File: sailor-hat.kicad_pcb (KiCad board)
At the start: 2 copper layers, 65 x 56 mm, 96 parts, among them J1 Screw_Terminal_01x04, J2 Raspberry_Pi_2_3, J3 Conn_02x07_Counter_Clockwise, J4 Screw_Terminal_01x02, J5 Screw_Terminal_01x03, J6 Conn_02x02_Odd_Even, Q1 DMP3098L, SW1 SW_SPST, U1 ATtiny841-SSU, U2 TPS61022, U3 H7533-H#, U4 DS3231MZ, U5 MCP2515-xST, U6 ISO1050DUB, U7 H7550-H#, U8 TX4138, Y1 1C208000BC0R

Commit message: Cram all new stuff on the PCB
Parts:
- removed D14: PSBD521S-40, Diode_SMD:D_SOD-523
- removed J6: Conn_02x02_Odd_Even, Connector_PinHeader_2.54mm:PinHeader_2x02_P2.54mm_Vertical
- removed R29, R30: 13k, Resistor_SMD:R_0603_1608Metric
- removed R31: 100k, Resistor_SMD:R_0603_1608Metric
- added C15: 2.2uF 16V, Capacitor_SMD:C_0603_1608Metric, F.Cu at (34.3, 67.4)
- added D10: SMBJ36CA, Diode_SMD:D_SMB, F.Cu at (38.4, 57.3)
- added D6: RB521S-30, Diode_SMD:D_SOD-523, F.Cu at (48.9, 59.3)
- added JP2: Jumper_2_Open, Connector_PinHeader_2.54mm:PinHeader_1x02_P2.54mm_Vertical, F.Cu at (36.5, 53.2)
- added JP3: Jumper_2_Open, Connector_PinHeader_2.54mm:PinHeader_1x02_P2.54mm_Vertical, F.Cu at (40.2, 53.2)
- added R22: 15k, Resistor_SMD:R_0603_1608Metric, F.Cu at (46.6, 58.4)
- added R25: 7.5k, Resistor_SMD:R_0603_1608Metric, F.Cu at (46.6, 59.9)
- added U9: INA199A1DCKR, Package_TO_SOT_SMD:SOT-363_SC-70-6_Handsoldering, F.Cu at (47.0, 38.0)
- C11: value 2.2uF 16V -> 2.2uF 50V; footprint Capacitor_SMD:C_0603_1608Metric -> Capacitor_SMD:C_1206_3216Metric
- C4: value 22pF -> 12pF
- C7: value 220pF -> 100nF
- C8: value 2.2uF 50V -> 1nF; footprint Capacitor_SMD:C_1206_3216Metric -> Capacitor_SMD:C_0603_1608Metric
- D1: value 5.0SMDJ20CA -> 5.0SMDJ36CA
- D13: value SMBJ20CA -> SS210; footprint Diode_SMD:D_SMB -> Diode_SMD:D_SMA
- D8: value MM3Z10 -> MM3Z8V2
- Q1: value DMP3098L -> WST03P06
- R17: value 13k -> 39k
- R20: value 100k -> 200k
- moved R23 13.6 mm to (47.1, 40.8), turned to 0 degrees
- moved C8 12.1 mm to (46.6, 61.5), turned to 180 degrees
- moved C7 11.0 mm to (47.2, 35.8)
- moved G*** 6.41 mm to (55.6, 63.2)
- moved C11 5.07 mm to (33.5, 60.8), turned to 90 degrees
- moved C27 4.84 mm to (73.7, 50.7), turned to 0 degrees
- moved U4 4.58 mm to (72.3, 55.1)
- moved L2 3.06 mm to (37.8, 37.3)
- moved D13 2.89 mm to (38.4, 61.4), turned to 0 degrees
- moved R20 2.69 mm to (53.3, 31.2), turned to 0 degrees
- moved C19 2.17 mm to (37.3, 31.9)
- moved R16 2.17 mm to (34.7, 30.5)
- moved C13 2.07 mm to (56.9, 49.1)
- moved F2 2.04 mm to (33.3, 54.5), turned to 90 degrees
- moved U2 1.80 mm to (41.0, 31.6)
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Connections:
- C10 pad 1: /CANbus interface/CAN_5V -> /CAN_5V
- C11 pad 1: /CANbus interface/CAN_5V -> /Protection/CAN12V_prot
- C16 pad 1: /Vcap -> /Buck converter/Vout
- C4 pad 1: /Vcap -> /Buck converter/Vout
- C7 pad 1: 5V -> GND
- C7 pad 2: /Boost converter/FB -> REG3.3V
- C8 pad 1: /CANbus interface/CAN12V_prot -> Net-(C8-Pad1)
- C8 pad 2: /CAN0_GND -> GND
- D13 pad 1: /CANbus interface/CAN12V_fused -> /Protection/CAN12V_prot
- D13 pad 2: /CAN0_GND -> /Protection/CAN12V_fused
- F2 pad 1: /CANbus interface/CAN12V_fused -> /Protection/CAN12V_fused
- L1 pad 2: /Vcap -> /Buck converter/Vout
- R14 pad 1: /Vcap -> /Buck converter/Vout
- R17 pad 2: Net-(R17-Pad2) -> GND
- R20 pad 1: Net-(R20-Pad1) -> /Vcap
- R23 pad 1: /Buck converter/ILIM -> /Vcap
- R23 pad 2: /Control MCU/12V_prot -> /Buck converter/Vout
- U6 pad 8: /CANbus interface/CAN_5V -> /CAN_5V
- U7 pad 2: /CANbus interface/CAN_5V -> /CAN_5V
- U7 pad 3: /CANbus interface/CAN12V_prot -> /Protection/CAN12V_prot
- U8 pad 2: /Buck converter/ILIM -> /Control MCU/12V_prot
- U8 pad 9: /Buck converter/ILIM -> /Control MCU/12V_prot
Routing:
- net REG3.3V: track 25.1 -> 68.6 mm, vias 2 -> 7
- net /Buck converter/Vout: track 0.00 -> 39.0 mm, vias 0 -> 6
- net /Vcap: track 76.7 -> 50.0 mm, vias 2 -> 4
- net /Buck converter/CSAOUT: track 0.00 -> 25.6 mm, vias 0 -> 3
- net /Buck converter/FB: track 5.85 -> 24.1 mm, vias 0 -> 2
- net GND: track 115.5 -> 130.4 mm
- net /CANbus interface/CAN_5V: track 11.3 -> 0.00 mm, vias 2 -> 0
- net /CAN_5V: track 0.00 -> 9.79 mm, vias 0 -> 2
- net /Protection/CAN12V_fused: track 0.00 -> 9.39 mm
- net /V12s: track 58.2 -> 66.6 mm, vias 5 -> 7
- net /CANbus interface/CAN12V_fused: track 6.37 -> 0.00 mm
- net /Control MCU/12V_prot: track 24.7 -> 30.7 mm, vias 0 -> 2
- net 3.3V: track 129.3 -> 123.5 mm, vias 8 -> 7
- net Net-(C8-Pad1): track 0.00 -> 5.32 mm
- net /CANbus interface/CAN12V_prot: track 5.27 -> 0.00 mm
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- added copper zone on B.Cu, net /Control MCU/12V_prot
- removed copper zone on B.Cu, net /Buck converter/ILIM
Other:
- board text added: "Rev.K"
- board text added: "Status"
- board text added: "Vcap"
- board text removed: "Rev.J"
- board text removed: "STA1"
- board text removed: "STA2"

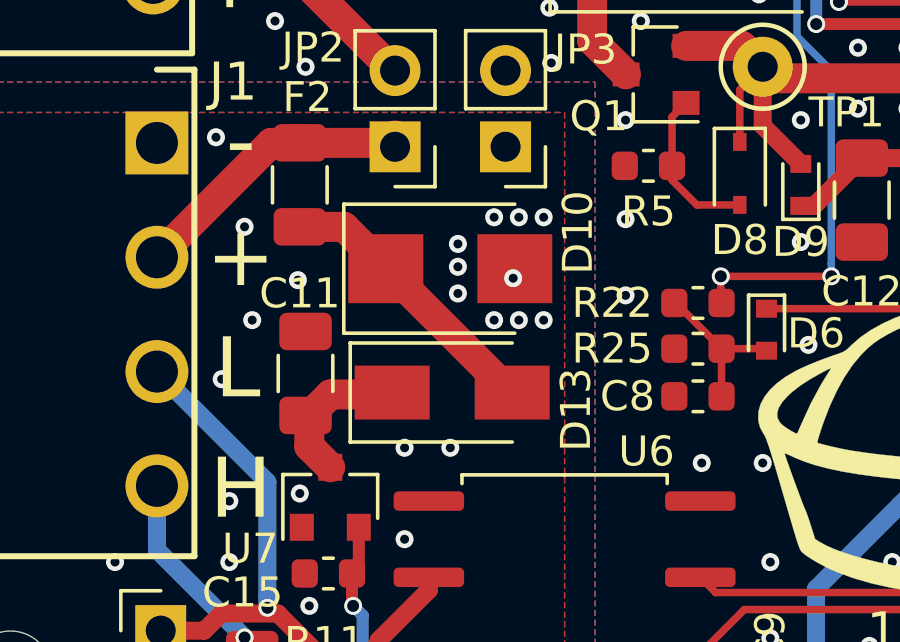
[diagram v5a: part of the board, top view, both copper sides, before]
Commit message: Swap CAN power rectifier diode into a smaller one
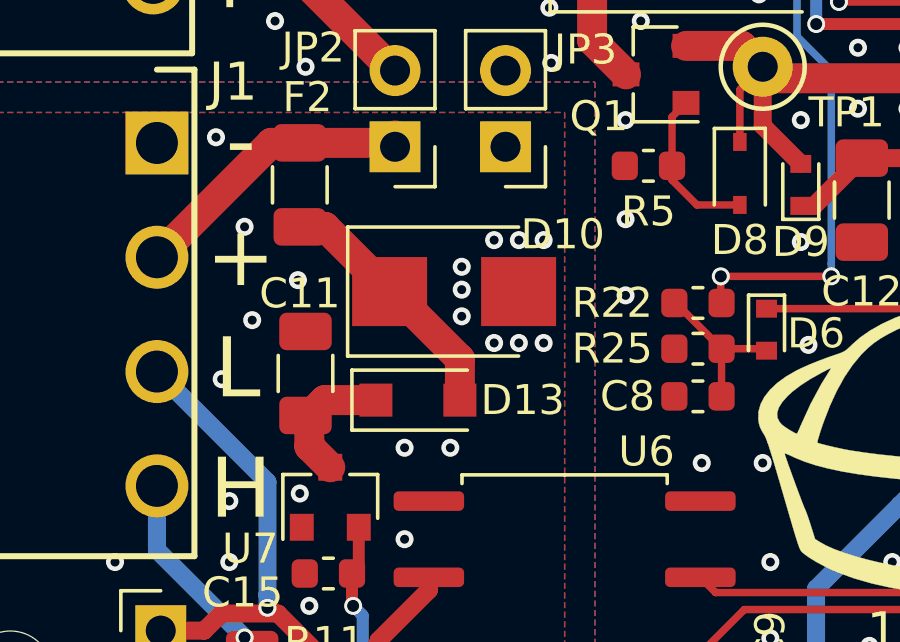
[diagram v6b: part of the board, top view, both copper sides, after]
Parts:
- D13: value SS210 -> SM4007PL; footprint Diode_SMD:D_SMA -> Diode_SMD:D_SOD-123F
- moved D13 1.17 mm to (37.3, 61.7)
- moved D10 0.77 mm to (38.5, 58.0)
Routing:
- net /Protection/CAN12V_fused: track 9.39 -> 8.53 mm
- net /Protection/CAN12V_prot: track 5.07 -> 4.45 mm
- net /CAN0_GND: vias 26 -> 25

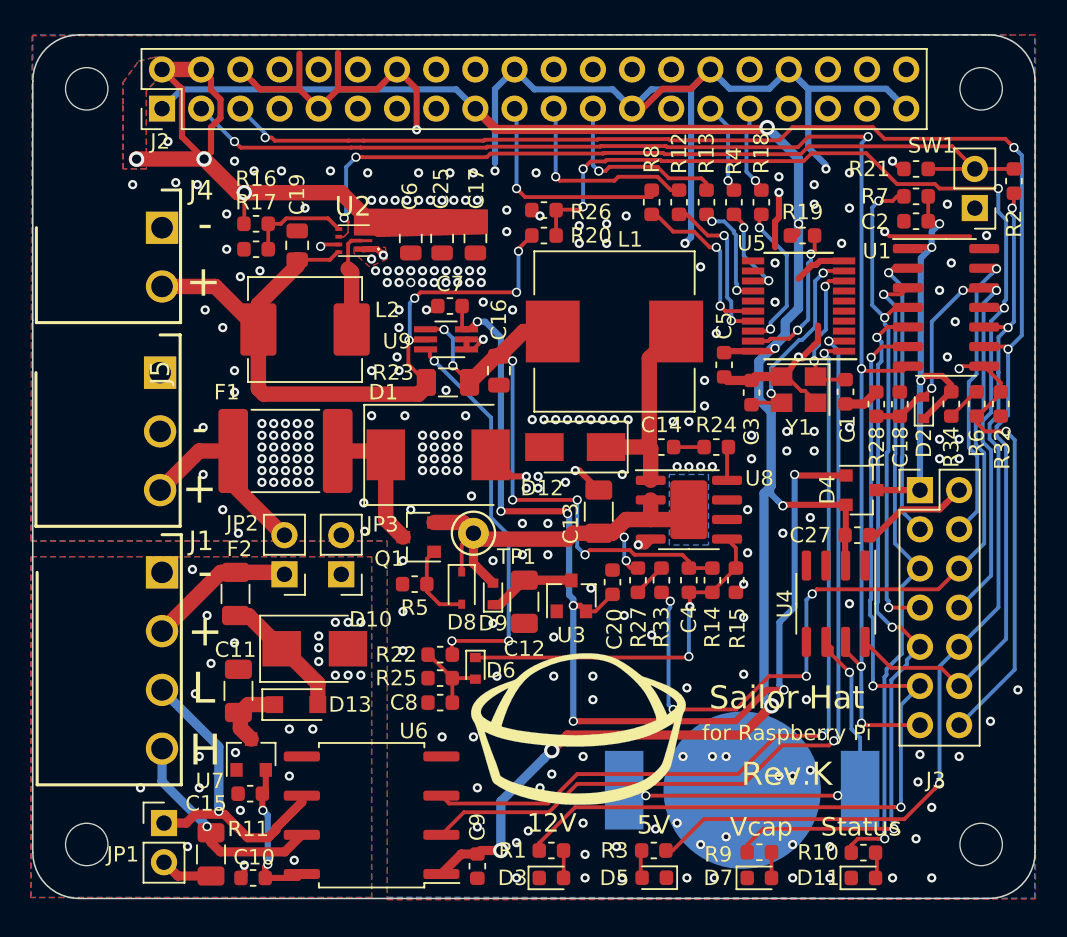
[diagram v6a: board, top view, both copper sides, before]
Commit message: Update components according to JLCPCB availability
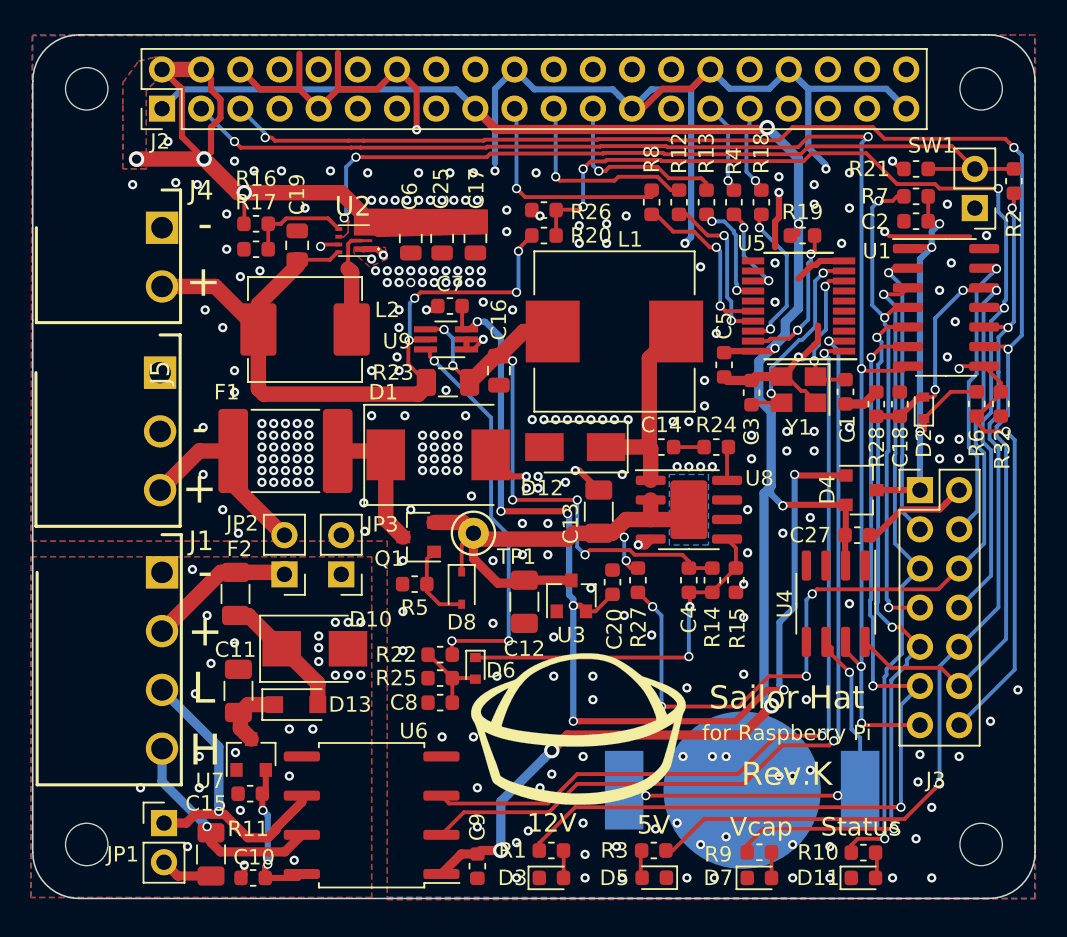
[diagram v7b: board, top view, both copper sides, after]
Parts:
- removed D9: PSBD521S-40, Diode_SMD:D_SOD-523
- removed R33, R34: 100k, Resistor_SMD:R_0603_1608Metric
- D1: value 5.0SMDJ36CA -> 5.0SMDJ33CA
- D10: value SMBJ36CA -> SMBJ33CA
- D6: value RB521S-30 -> PSBD521S-40
- R27: value 100k -> 62k
- R28: value 13k -> 2.2k
- R6: value 100k -> 200k
- Y1: value 1C208000BC0R -> 1C208000CE0Q
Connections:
- C12 pad 1: Net-(C12-Pad1) -> /Control MCU/12V_prot
- R27 pad 2: Net-(R27-Pad2) -> /V12s
- R6 pad 1: Net-(R34-Pad2) -> /ATT_Vcc
- U3 pad 3: Net-(C12-Pad1) -> /Control MCU/12V_prot
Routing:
- net Net-(C12-Pad1): track 5.75 -> 0.00 mm
- net /Control MCU/12V_prot: track 30.7 -> 35.7 mm
- net Net-(R34-Pad2): track 2.30 -> 0.00 mm
- net Net-(R27-Pad2): track 2.21 -> 0.00 mm
- net /V12s: track 66.6 -> 67.8 mm

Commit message: Redesigned layout to take EMC issues better into account
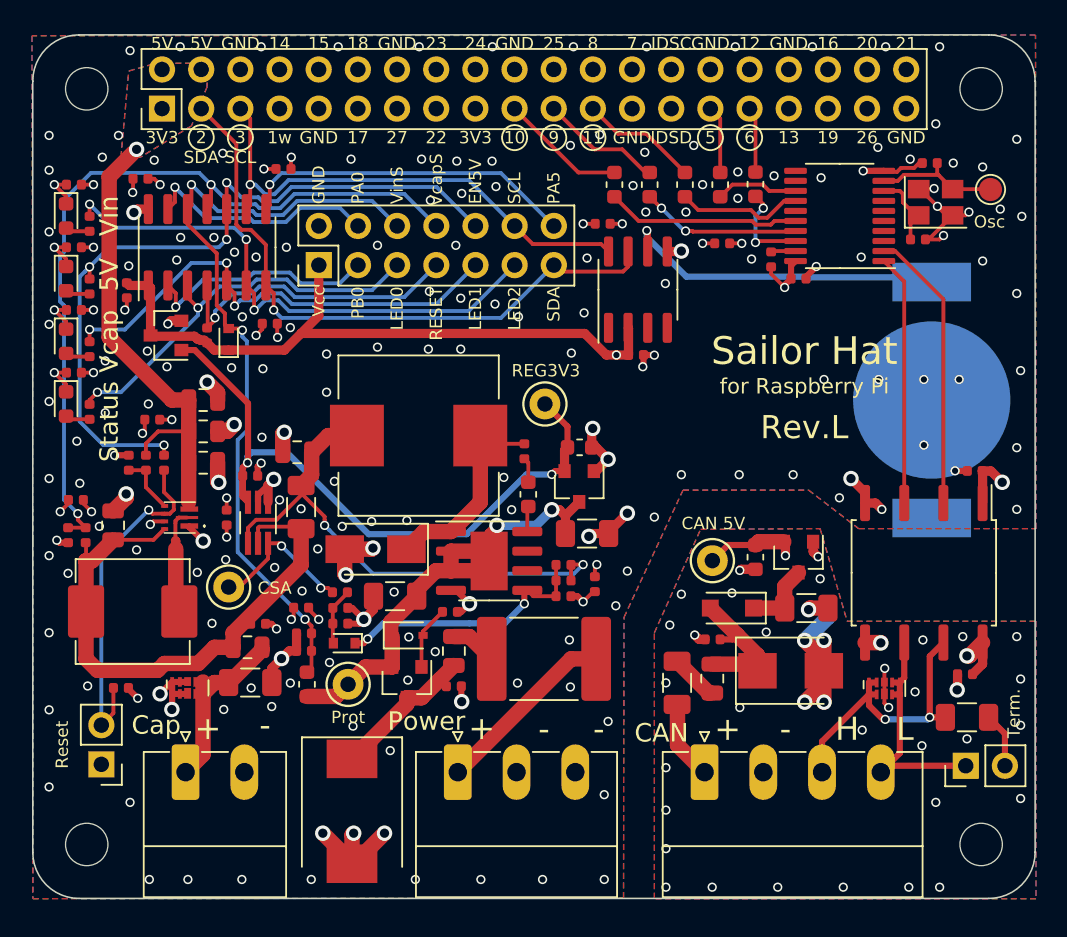
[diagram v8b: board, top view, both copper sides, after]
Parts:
- removed BT1: CR1220 3V, custom:BatteryHolder_Linx_BAT-HLD-012-SMT
- removed C1, C3: 22pF, Capacitor_SMD:C_0603_1608Metric
- removed C10, C14, C18, C2, C27, C5, C7, C9: 100nF, Capacitor_SMD:C_0603_1608Metric
- removed C11, C12: 2.2uF 50V, Capacitor_SMD:C_1206_3216Metric
- removed C13: 10uF 50V, Capacitor_SMD:C_1206_3216Metric
- removed C15, C20: 2.2uF 16V, Capacitor_SMD:C_0603_1608Metric
- removed C16, C17, C19, C25, C6: 22uF 6.3V, Capacitor_SMD:C_0805_2012Metric
- removed C4: 12pF, Capacitor_SMD:C_0603_1608Metric
- removed C8: 1nF, Capacitor_SMD:C_0603_1608Metric
- removed D1: 5.0SMDJ33CA, Diode_SMD:D_SMC
- removed D10: SMBJ33CA, Diode_SMD:D_SMB
- removed D11, D5: RLED, LED_SMD:LED_0603_1608Metric
- removed D12: SS54F, Diode_SMD:D_SMA
- removed D13: SM4007PL, Diode_SMD:D_SOD-123F
- removed D2, D6: PSBD521S-40, Diode_SMD:D_SOD-523
- removed D3, D7: GLED, LED_SMD:LED_0603_1608Metric
- removed D4: BAT54C, Package_TO_SOT_SMD:SOT-23
- removed D8: MM3Z8V2, Diode_SMD:D_SOD-323
- removed F1: ASMD2920-185, Fuse:Fuse_2920_7451Metric
- removed F2: SMD1206P010TF, Fuse:Fuse_1206_3216Metric
- removed the G*** at (55.6, 63.2)
- removed J1: Screw_Terminal_01x04, custom:TerminalBlock_WJ15EDGRC-3.81-4P
- removed J2: Raspberry_Pi_2_3, Connector_PinHeader_2.54mm:PinHeader_2x20_P2.54mm_Vertical
- removed J3: Conn_02x07_Counter_Clockwise, custom:PinHeader_2x07_P2.54mm_Vertical_CounterClockwise
- removed J4: Screw_Terminal_01x02, custom:TerminalBlock_WJ15EDGRC-3.81-2P
- removed J5: Screw_Terminal_01x03, custom:TerminalBlock_WJ15EDGRC-3.81-3P
- removed JP1: Term, Connector_PinHeader_2.54mm:PinHeader_1x02_P2.54mm_Vertical
- removed JP2, JP3: Jumper_2_Open, Connector_PinHeader_2.54mm:PinHeader_1x02_P2.54mm_Vertical
- removed L1: MWSA1004-150MT, Inductor_SMD:L_Wuerth_HCI-1040
- removed L2: MWSA0603-1R0MT, Inductor_SMD:L_Abracon_ASPI-0630LR
- removed Q1: WST03P06, Package_TO_SOT_SMD:SOT-23
- removed R1, R10, R28, R3, R9: 2.2k, Resistor_SMD:R_0603_1608Metric
- removed R11: 120R, Resistor_SMD:R_1206_3216Metric
- removed R12, R13, R18, R4, R8: 0, Resistor_SMD:R_0603_1608Metric
- removed R14, R16: 300k, Resistor_SMD:R_0603_1608Metric
- removed R15, R26: 130k, Resistor_SMD:R_0603_1608Metric
- removed R17: 39k, Resistor_SMD:R_0603_1608Metric
- removed R19, R2, R7: 10k, Resistor_SMD:R_0603_1608Metric
- removed R20, R6: 200k, Resistor_SMD:R_0603_1608Metric
- removed R21, R32, R5: 100k, Resistor_SMD:R_0603_1608Metric
- removed R22: 15k, Resistor_SMD:R_0603_1608Metric
- removed R23: 20m, Resistor_SMD:R_1206_3216Metric
- removed R24: 5.1, Resistor_SMD:R_0603_1608Metric
- removed R25: 7.5k, Resistor_SMD:R_0603_1608Metric
- removed R27: 62k, Resistor_SMD:R_0603_1608Metric
- removed SW1: SW_SPST, Connector_PinHeader_2.54mm:PinHeader_1x02_P2.54mm_Vertical
- removed TP1: +12V_prot, TestPoint:TestPoint_Keystone_5000-5004_Miniature
- removed U1: ATtiny841-SSU, Package_SO:SOIC-14_3.9x8.7mm_P1.27mm
- removed U2: TPS61022, custom:TPS61022RWUR
- removed U3: H7533-H#, Package_TO_SOT_SMD:SOT-23
- removed U4: DS3231MZ, Package_SO:SOIC-8_3.9x4.9mm_P1.27mm
- removed U5: MCP2515-xST, Package_SO:TSSOP-20_4.4x6.5mm_P0.65mm
- removed U6: ISO1050DUB, Package_SO:SOP-8_6.62x9.15mm_P2.54mm
- removed U7: H7550-H#, Package_TO_SOT_SMD:SOT-23
- removed U8: TX4138, Package_SO:SOIC-8-1EP_3.9x4.9mm_P1.27mm_EP2.41x3.81mm
- removed U9: INA199A1DCKR, Package_TO_SOT_SMD:SOT-363_SC-70-6_Handsoldering
- removed Y1: 1C208000CE0Q, Crystal:Crystal_SMD_3225-4Pin_3.2x2.5mm
- added BT401: CR1220/3V, custom:BatteryHolder_Linx_BAT-HLD-012-SMT, B.Cu at (78.5, 41.9)
- added C201: 22uF/6.3V, Capacitor_SMD:C_0805_2012Metric, F.Cu at (25.4, 50.0)
- added C202: 22uF/6.3V, Capacitor_SMD:C_0805_2012Metric, F.Cu at (31.2, 46.0)
- added C203: 22uF/6.3V, Capacitor_SMD:C_0805_2012Metric, F.Cu at (31.2, 41.9)
- added C204: 22uF/6.3V, Capacitor_SMD:C_0805_2012Metric, F.Cu at (31.2, 43.9)
- added C301: 10uF/50V, Capacitor_SMD:C_1206_3216Metric, F.Cu at (43.7, 54.6)
- added C302: 2.2uF/50V, Capacitor_SMD:C_1206_3216Metric, F.Cu at (56.1, 50.6)
- added C303: 2.2uF/16V, Capacitor_SMD:C_0603_1608Metric, F.Cu at (55.7, 45.0)
- added C304: 100nF, Capacitor_SMD:C_0402_1005Metric, F.Cu at (52.1, 45.2)
- added C305: 22uF/6.3V, Capacitor_SMD:C_0805_2012Metric, F.Cu at (37.3, 45.3)
- added C306: 12pF, Capacitor_SMD:C_0402_1005Metric, F.Cu at (54.6, 52.6)
- added C307: 100nF, Capacitor_SMD:C_0402_1005Metric, F.Cu at (34.3, 46.8)
- added C308: 1nF, Capacitor_SMD:C_0402_1005Metric, F.Cu at (40.1, 55.4)
- added C401: 100nF, Capacitor_SMD:C_0402_1005Metric, F.Cu at (59.3, 39.0)
- added C501: 10nF/50V, Capacitor_SMD:C_0402_1005Metric, F.Cu at (47.5, 60.5)
- added C601: 100nF, Capacitor_SMD:C_0402_1005Metric, F.Cu at (37.8, 57.0)
- added C602: 100nF, Capacitor_SMD:C_0402_1005Metric, F.Cu at (26.3, 34.8)
- added C701: 10uF/50V, Capacitor_SMD:C_1206_3216Metric, F.Cu at (34.3, 60.2)
- added C702: 10uF, Capacitor_SMD:C_0402_1005Metric, F.Cu at (34.8, 56.4)
- added C801: 10nF/50V, Capacitor_SMD:C_0402_1005Metric, F.Cu at (64.3, 57.4)
- added C802: 2.2uF/50V, Capacitor_SMD:C_1206_3216Metric, F.Cu at (70.4, 55.4)
- added C803: 22pF, Capacitor_SMD:C_0402_1005Metric, F.Cu at (77.6, 31.5)
- added C804: 22pF, Capacitor_SMD:C_0402_1005Metric, F.Cu at (78.4, 26.5)
- added C805: 2.2uF/16V, Capacitor_SMD:C_0603_1608Metric, F.Cu at (67.1, 52.1)
- added C806: 100nF, Capacitor_SMD:C_0402_1005Metric, F.Cu at (69.8, 34.0)
- added C807: 100nF, Capacitor_SMD:C_0402_1005Metric, F.Cu at (81.3, 46.5)
- added C808: 100nF, Capacitor_SMD:C_0402_1005Metric, F.Cu at (80.6, 59.7)
- added C901: 100nF, Capacitor_SMD:C_0402_1005Metric, F.Cu at (22.9, 27.9)
- added C902: 100nF, Capacitor_SMD:C_0402_1005Metric, F.Cu at (23.0, 48.4)
- added C903: 100nF, Capacitor_SMD:C_0402_1005Metric, F.Cu at (27.9, 43.2)
- added C904: 100nF, Capacitor_SMD:C_0402_1005Metric, F.Cu at (27.2, 27.6)
- added C905: 100nF, Capacitor_SMD:C_0402_1005Metric, F.Cu at (35.6, 37.0)
- added C906: 100nF, Capacitor_SMD:C_0402_1005Metric, F.Cu at (64.9, 31.8)
- added C907: 100nF, Capacitor_SMD:C_0402_1005Metric, F.Cu at (37.6, 55.4)
- added C908: 100nF, Capacitor_SMD:C_0402_1005Metric, F.Cu at (56.6, 53.8)
- added C909: 100nF, Capacitor_SMD:C_0402_1005Metric, F.Cu at (57.1, 30.5)
- added C910: 100nF, Capacitor_SMD:C_0402_1005Metric, F.Cu at (36.4, 26.9)
- added C911: 100nF, Capacitor_SMD:C_0402_1005Metric, F.Cu at (22.9, 32.0)
- added C912: 100nF, Capacitor_SMD:C_0402_1005Metric, F.Cu at (22.9, 36.1)
- added C913: 100nF, Capacitor_SMD:C_0402_1005Metric, F.Cu at (22.9, 40.1)
- added C914: 100nF, Capacitor_SMD:C_0402_1005Metric, F.Cu at (32.8, 49.5)
- added D301: SS54F, Diode_SMD:D_SMA, F.Cu at (42.4, 51.6)
- added D302: PSBD521S-40, Diode_SMD:D_SOD-523, F.Cu at (40.4, 57.7)
- added D501: 5.0SMDJ33CA, Diode_SMD:D_SMC, F.Cu at (40.9, 68.6)
- added D502: MM3Z8V2, Diode_SMD:D_SOD-323, F.Cu at (44.5, 57.2)
- added D601: PSBD521S-40, Diode_SMD:D_SOD-523, F.Cu at (32.9, 38.0)
- added D602: BAT54C, Package_TO_SOT_SMD:SOT-23, F.Cu at (28.8, 37.7)
- added D701: GLED, LED_SMD:LED_0603_1608Metric, F.Cu at (22.4, 30.0)
- added D702: RLED, LED_SMD:LED_0603_1608Metric, F.Cu at (22.4, 34.0)
- added D703: GLED, LED_SMD:LED_0603_1608Metric, F.Cu at (22.4, 38.1)
- added D704: RLED, LED_SMD:LED_0603_1608Metric, F.Cu at (22.4, 42.2)
- added D801: SMBJ33CA, Diode_SMD:D_SMB, F.Cu at (69.3, 59.5)
- added D802: SM4007PL, Diode_SMD:D_SOD-123F, F.Cu at (65.5, 55.4)
- added F501: ASMD2920-185, Fuse:Fuse_2920_7451Metric, F.Cu at (53.3, 58.7)
- added F801: SMD1206P010TF, Fuse:Fuse_1206_3216Metric, F.Cu at (62.0, 60.2)
- added FB501: GZ2012D601TF, Inductor_SMD:L_0805_2012Metric, F.Cu at (47.5, 58.2)
- added FB701: GZ2012D601TF, Inductor_SMD:L_0805_2012Metric, F.Cu at (34.1, 57.9)
- added FB801: GZ2012D601TF, Inductor_SMD:L_0805_2012Metric, F.Cu at (64.3, 60.0)
- added J501: Screw_Terminal_01x03, Connector_Phoenix_MC:PhoenixContact_MC_1,5_3-G-3.81_1x03_P3.81mm_Horizontal, F.Cu at (47.8, 66.0)
- added J601: Conn_02x07_Counter_Clockwise, custom:PinHeader_2x07_P2.54mm_Vertical_CounterClockwise, F.Cu at (38.7, 33.2)
- added J701: Screw_Terminal_01x02, Connector_Phoenix_MC:PhoenixContact_MC_1,5_2-G-3.81_1x02_P3.81mm_Horizontal, F.Cu at (30.1, 66.0)
- added J702: Raspberry_Pi_2_3, Connector_PinHeader_2.54mm:PinHeader_2x20_P2.54mm_Vertical, F.Cu at (28.6, 23.0)
- added J801: Screw_Terminal_01x04, Connector_Phoenix_MC:PhoenixContact_MC_1,5_4-G-3.81_1x04_P3.81mm_Horizontal, F.Cu at (63.8, 66.0)
- added JP801: Term, Connector_PinHeader_2.54mm:PinHeader_1x02_P2.54mm_Vertical, F.Cu at (80.7, 65.6)
- added L201: MWSA0603-1R0MT, Inductor_SMD:L_Abracon_ASPI-0630LR, F.Cu at (26.7, 55.6)
- added L301: MWSA1004-150MT, Inductor_SMD:L_Wuerth_HCI-1040, F.Cu at (45.2, 44.2)
- added Q501: WST03P06, Package_TO_SOT_SMD:SOT-23, F.Cu at (44.5, 60.2)
- added R201: 10k, Resistor_SMD:R_0402_1005Metric, F.Cu at (28.7, 46.0)
- added R202: 100k, Resistor_SMD:R_0402_1005Metric, F.Cu at (25.9, 60.6)
- added R203: 300k, Resistor_SMD:R_0402_1005Metric, F.Cu at (27.5, 46.0)
- added R204: 39k, Resistor_SMD:R_0402_1005Metric, F.Cu at (26.4, 46.0)
- added R301: 5.1, Resistor_SMD:R_0603_1608Metric, F.Cu at (52.3, 48.0)
- added R302: 470k, Resistor_SMD:R_0402_1005Metric, F.Cu at (54.6, 53.6)
- added R303: 220k, Resistor_SMD:R_0402_1005Metric, F.Cu at (54.6, 54.6)
- added R304: 20m, Resistor_SMD:R_1206_3216Metric, F.Cu at (37.6, 48.9)
- added R305: 15k, Resistor_SMD:R_0402_1005Metric, F.Cu at (40.1, 54.4)
- added R306: 7.5k, Resistor_SMD:R_0402_1005Metric, F.Cu at (40.1, 56.4)
- added R501: 100k, Resistor_SMD:R_0402_1005Metric, F.Cu at (47.2, 55.6)
- added R601: 62k, Resistor_SMD:R_0603_1608Metric, F.Cu at (38.0, 60.3)
- added R602: 2.2k, Resistor_SMD:R_0402_1005Metric, F.Cu at (37.8, 58.2)
- added R603: 10k, Resistor_SMD:R_0402_1005Metric, F.Cu at (31.5, 37.7)
- added R604: 300k, Resistor_SMD:R_0402_1005Metric, F.Cu at (23.6, 50.7)
- added R605: 200k, Resistor_SMD:R_0402_1005Metric, F.Cu at (22.5, 50.7)
- added R701: 2.2k, Resistor_SMD:R_0402_1005Metric, F.Cu at (23.9, 30.5)
- added R702: 2.2k, Resistor_SMD:R_0402_1005Metric, F.Cu at (23.9, 34.5)
- added R703: 2.2k, Resistor_SMD:R_0402_1005Metric, F.Cu at (23.9, 38.6)
- added R704: 2.2k, Resistor_SMD:R_0402_1005Metric, F.Cu at (23.9, 42.7)
- added R705: 0, Resistor_SMD:R_0603_1608Metric, F.Cu at (57.9, 27.9)
- added R706: 0, Resistor_SMD:R_0603_1608Metric, F.Cu at (60.2, 27.9)
- added R707: 0, Resistor_SMD:R_0603_1608Metric, F.Cu at (62.5, 27.9)
- added R708: 0, Resistor_SMD:R_0603_1608Metric, F.Cu at (67.1, 27.9)
- added R709: 0, Resistor_SMD:R_0603_1608Metric, F.Cu at (64.8, 27.9)
- added R801: 120R, Resistor_SMD:R_1206_3216Metric, F.Cu at (80.8, 62.5)
- added R802: 10k, Resistor_SMD:R_0402_1005Metric, F.Cu at (68.1, 32.8)
- added SW201: SW_SPST, Connector_PinHeader_2.54mm:PinHeader_1x02_P2.54mm_Vertical, F.Cu at (24.6, 65.5)
- added TP301: REG3.3V, TestPoint:TestPoint_Keystone_5000-5004_Miniature, F.Cu at (53.4, 42.2)
- added TP302: CSA, TestPoint:TestPoint_Keystone_5000-5004_Miniature, F.Cu at (32.9, 54.0)
- added TP501: Vin_prot, TestPoint:TestPoint_Keystone_5000-5004_Miniature, F.Cu at (40.6, 60.3)
- added TP801: OSC1, TestPoint:TestPoint_Pad_D1.5mm, F.Cu at (82.3, 28.3)
- added TP802: CAN_5V, TestPoint:TestPoint_Keystone_5000-5004_Miniature, F.Cu at (64.3, 52.3)
- added U201: TPS61022, custom:TPS61022RWUR, F.Cu at (29.7, 49.5)
- added U301: H7533-H#, Package_TO_SOT_SMD:SOT-23, F.Cu at (55.6, 47.5)
- added U302: TX4138, Package_SO:SOIC-8-1EP_3.9x4.9mm_P1.27mm_EP2.41x3.81mm, F.Cu at (49.8, 52.3)
- added U303: INA199A1DCKR, Package_TO_SOT_SMD:SOT-363_SC-70-6_Handsoldering, F.Cu at (34.8, 49.9)
- added U401: DS3231MZ, Package_SO:SOIC-8_3.9x4.9mm_P1.27mm, F.Cu at (59.4, 34.8)
- added U601: ATtiny841-SSU, Package_SO:SOIC-14_3.9x8.7mm_P1.27mm, F.Cu at (31.5, 32.0)
- added U701: RCLAMP0524P-N, Package_DFN_QFN:Diodes_UDFN-10_1.0x2.5mm_P0.5mm, F.Cu at (30.2, 60.6)
- added U801: RCLAMP0524P-N, Package_DFN_QFN:Diodes_UDFN-10_1.0x2.5mm_P0.5mm, F.Cu at (75.4, 60.6)
- added U802: H7550-H#, Package_TO_SOT_SMD:SOT-23, F.Cu at (69.8, 52.1)
- added U803: MCP2515-xST, Package_SO:TSSOP-20_4.4x6.5mm_P0.65mm, F.Cu at (72.5, 30.0)
- added U804: ISO1050DUB, Package_SO:SOP-8_6.62x9.15mm_P2.54mm, F.Cu at (78.0, 53.1)
- added Y801: 1C208000CE0Q, Crystal:Crystal_SMD_3225-4Pin_3.2x2.5mm, F.Cu at (78.7, 29.1)
- moved G*** 43.5 mm to (28.4, 29.5)
- moved REF** 24.3 mm to (28.4, 40.9)
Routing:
- net 3.3V: track 123.5 -> 0.00 mm, vias 7 -> 0
- net /V12s: track 67.8 -> 0.00 mm, vias 7 -> 0
- net /SCL: track 98.4 -> 32.7 mm, vias 3 -> 1
- net /VcapS: track 64.8 -> 0.00 mm, vias 4 -> 0
- net /Control MCU/VcapS: track 0.00 -> 52.1 mm, vias 0 -> 2
- net /Control MCU/VinS: track 0.00 -> 51.3 mm, vias 0 -> 3
- net /SDA: track 92.0 -> 41.3 mm, vias 5 -> 1
- net GND: track 130.4 -> 93.5 mm, vias 256 -> 205
- net /CANbus interface/CAN_TX: track 53.2 -> 16.2 mm, vias 2 -> 0
- net /CANbus interface/CAN_RX: track 55.3 -> 18.4 mm, vias 2 -> 0
- net /Control MCU/12V_prot: track 35.7 -> 0.00 mm, vias 2 -> 0
- net /ATT_RESET: track 31.8 -> 0.00 mm, vias 3 -> 0
- net /Vin_prot: track 0.00 -> 31.5 mm, vias 0 -> 2
- net /Boost converter/ENIN: track 52.7 -> 22.6 mm, vias 2 -> 1
- net /PA5: track 29.5 -> 0.00 mm, vias 2 -> 0
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- added copper zone on In2.Cu, net +3V3
- added copper zone on B.Cu, net /CANbus interface/CAN0_GND
- added copper zone on F.Cu, net /CANbus interface/CAN0_GND
- added copper zone on In1.Cu, net /CANbus interface/CAN0_GND
- added copper zone on In2.Cu, net /CANbus interface/CAN0_GND
- added copper zone on In2.Cu, net /CANbus interface/CAN_5V
- added copper zone on In1.Cu, net GND
- added copper zone on In2.Cu, net GND
- removed copper zone on B.Cu, net /CAN0_GND
- removed copper zone on F.Cu, net /CAN0_GND
- removed copper zone on B.Cu, net /Control MCU/12V_prot
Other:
- copper layers 2 -> 4
- board text added: "10"
- board text added: "11"
- board text added: "12"
- board text added: "13"
- board text added: "14"
- board text added: "15"
- board text added: "16"
- board text added: "17"
- board text added: "18"
- board text added: "19"
- board text added: "1w"
- board text added: "2 SDA"
- board text added: "20"
- board text added: "21"
- board text added: "22"
- board text added: "23"
- board text added: "24"
- board text added: "25"
- board text added: "26"
- board text added: "27"
- board text added: "3 SCL"
- board text added: "3V3"
- board text added: "5"
- board text added: "6"
- board text added: "7"
- board text added: "8"
- board text added: "9"
- board text added: "CAN 5V"
- board text added: "CAN NMEA 2000"
- board text added: "CR1220 battery"
- board text added: "CSA"
- board text added: "Cap"
- board text added: "EN5V"
- board text added: "GND"
- board text added: "IDSC"
- board text added: "IDSD"
- board text added: "LED0"
- board text added: "LED1"
- board text added: "LED2"
- board text added: "Osc"
- board text added: "PA0"
- board text added: "PA5"
- board text added: "PB0"
- board text added: "Power"
- board text added: "Prot"
- board text added: "REG3V3"
- board text added: "RESET"
- board text added: "Reset"
- board text added: "Rev.L"
- board text added: "SCL"
- board text added: "SDA"
- board text added: "Term."
- board text added: "VcapS"
- board text added: "Vcc"
- board text added: "Vin"
- board text added: "VinS"
- board text removed: "12V"
- board text removed: "CAP"
- board text removed: "PWR"
- board text removed: "Rev.K"
- board text removed: "© Hat Laboratories, 2020"
